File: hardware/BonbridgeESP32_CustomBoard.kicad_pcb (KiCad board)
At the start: 2 copper layers, 55 x 25 mm, 13 parts, among them J1 RJ45_MagJack_10/100M, J2 USB-C_PROG, J3 24V_IN, J4 PRINTER_USB, U1 ESP32-S3-WROOM-1U (IPEX), U2 W5500, U3 Buck_24V_to_5V_3A, U4 LDO_3.3V_600mA

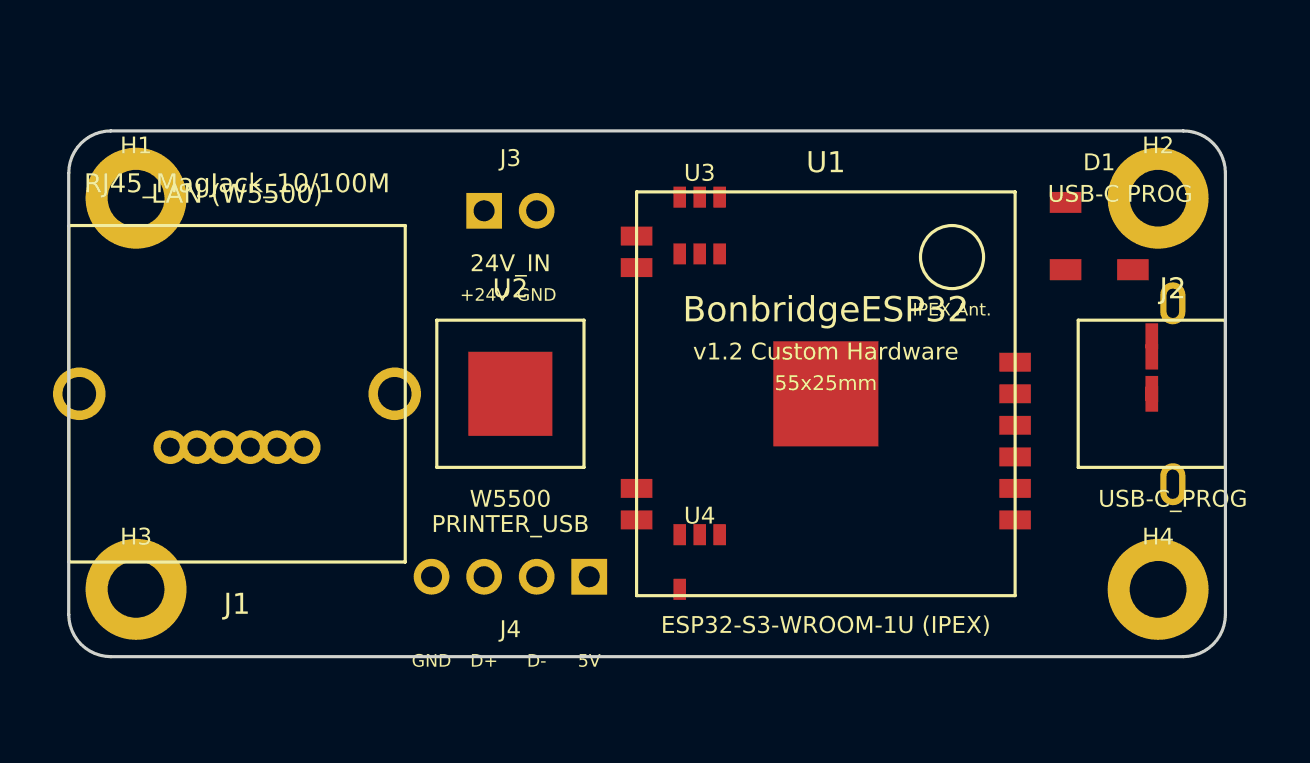
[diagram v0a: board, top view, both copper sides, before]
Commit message: hardware: update KiCad board layout (RJ45 on bottom long edge, USB-C opposite on top, JST top-left side by side)
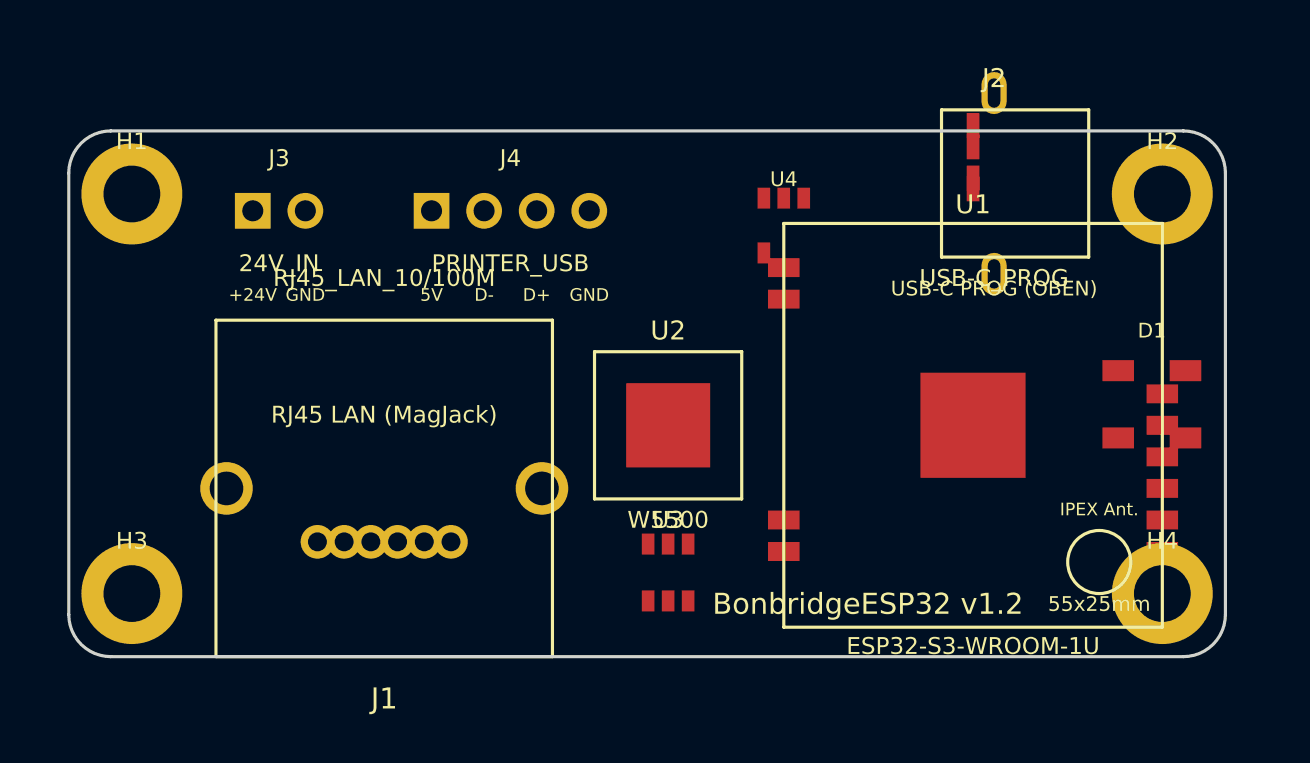
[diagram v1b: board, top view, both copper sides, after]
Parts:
- J1: value RJ45_MagJack_10/100M -> RJ45_LAN_10/100M
- U1: value ESP32-S3-WROOM-1U (IPEX) -> ESP32-S3-WROOM-1U
- moved J4 17.4 mm to (121.0, 103.8), turned to 0 degrees
- moved U3 16.6 mm to (128.5, 121.0)
- moved U4 16.5 mm to (134.0, 104.5)
- moved J2 13.1 mm to (144.0, 102.5), turned to 180 degrees
- moved J3 11.0 mm to (110.0, 103.8)
- moved D1 8.38 mm to (151.5, 113.0)
- moved J1 8.32 mm to (115.0, 117.0), turned to 90 degrees
- moved U2 7.65 mm to (128.5, 114.0)
- moved U1 7.16 mm to (143.0, 114.0)
- moved H1 0.28 mm to (103.0, 103.0)
- moved H3 0.28 mm to (103.0, 122.0)
- moved H2 0.28 mm to (152.0, 103.0)
- moved H4 0.28 mm to (152.0, 122.0)
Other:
- board text added: "BonbridgeESP32 v1.2"
- board text added: "RJ45 LAN (MagJack)"
- board text added: "USB-C PROG (OBEN)"
- board text removed: "BonbridgeESP32"
- board text removed: "LAN (W5500)"
- board text removed: "USB-C PROG"
- board text removed: "v1.2 Custom Hardware"

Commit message: hardware: fix KiCad 10 parsing error, add 3mm RJ45 overhang, and add 3D board renders
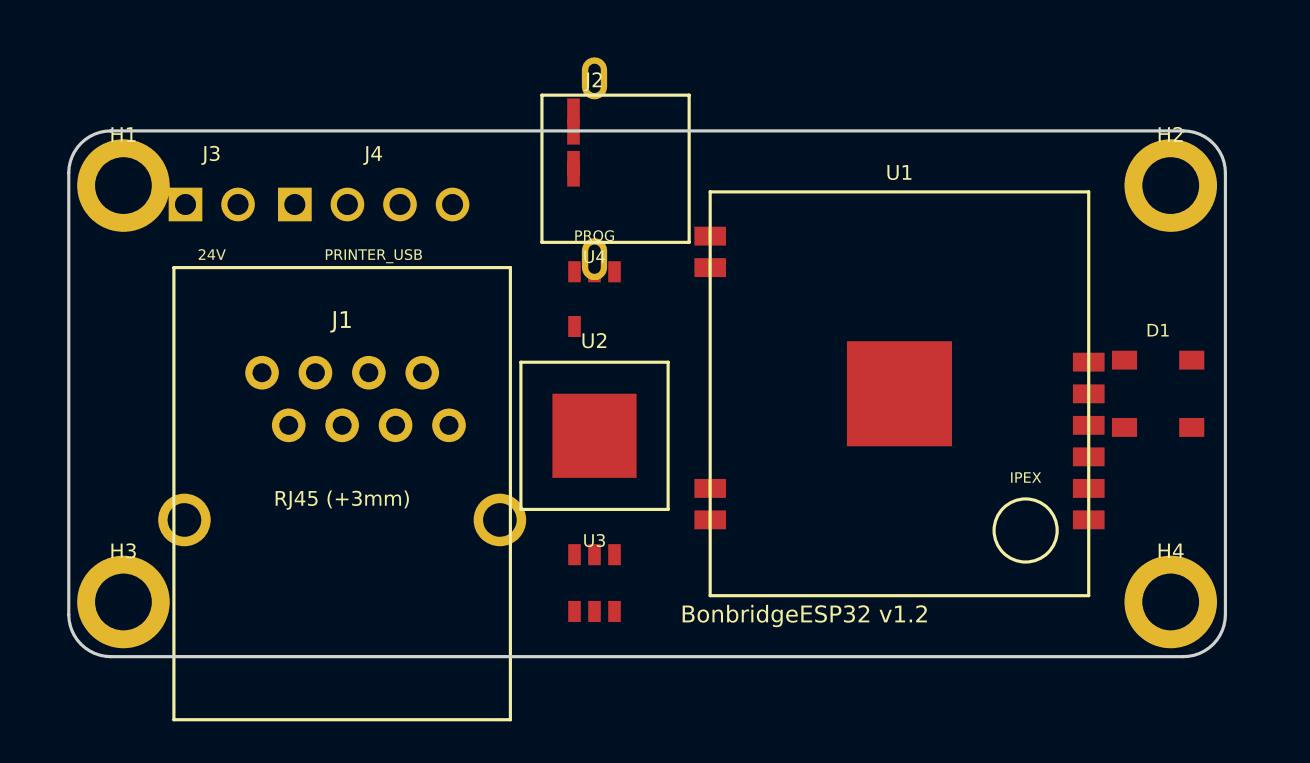
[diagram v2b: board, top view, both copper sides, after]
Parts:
- D1: value WS2812B (RGB) -> RGB
- J1: value RJ45_LAN_10/100M -> RJ45 (+3mm)
- J2: value USB-C_PROG -> PROG
- J3: value 24V_IN -> 24V
- U3: value Buck_24V_to_5V_3A -> Buck
- U4: value LDO_3.3V_600mA -> 3.3V
- moved J2 19.0 mm to (125.0, 101.8)
- moved U4 9.66 mm to (125.0, 108.0)
- moved J4 6.51 mm to (114.5, 103.5)
- moved U1 3.81 mm to (139.5, 112.5)
- moved U2 3.54 mm to (125.0, 114.5)
- moved U3 3.54 mm to (125.0, 121.5)
- moved J3 3.21 mm to (106.8, 103.5)
- moved J1 2.06 mm to (113.0, 117.5), turned to 0 degrees
- moved D1 0.58 mm to (151.8, 112.5)
- moved H1 0.57 mm to (102.6, 102.6)
- moved H2 0.57 mm to (152.4, 102.6)
- moved H3 0.57 mm to (102.6, 122.4)
- moved H4 0.57 mm to (152.4, 122.4)
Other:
- board text removed: "55x25mm"
- board text removed: "RJ45 LAN (MagJack)"
- board text removed: "USB-C PROG (OBEN)"

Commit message: feat(hardware): populate complete component layout with 0 DRC violations and 3D preview
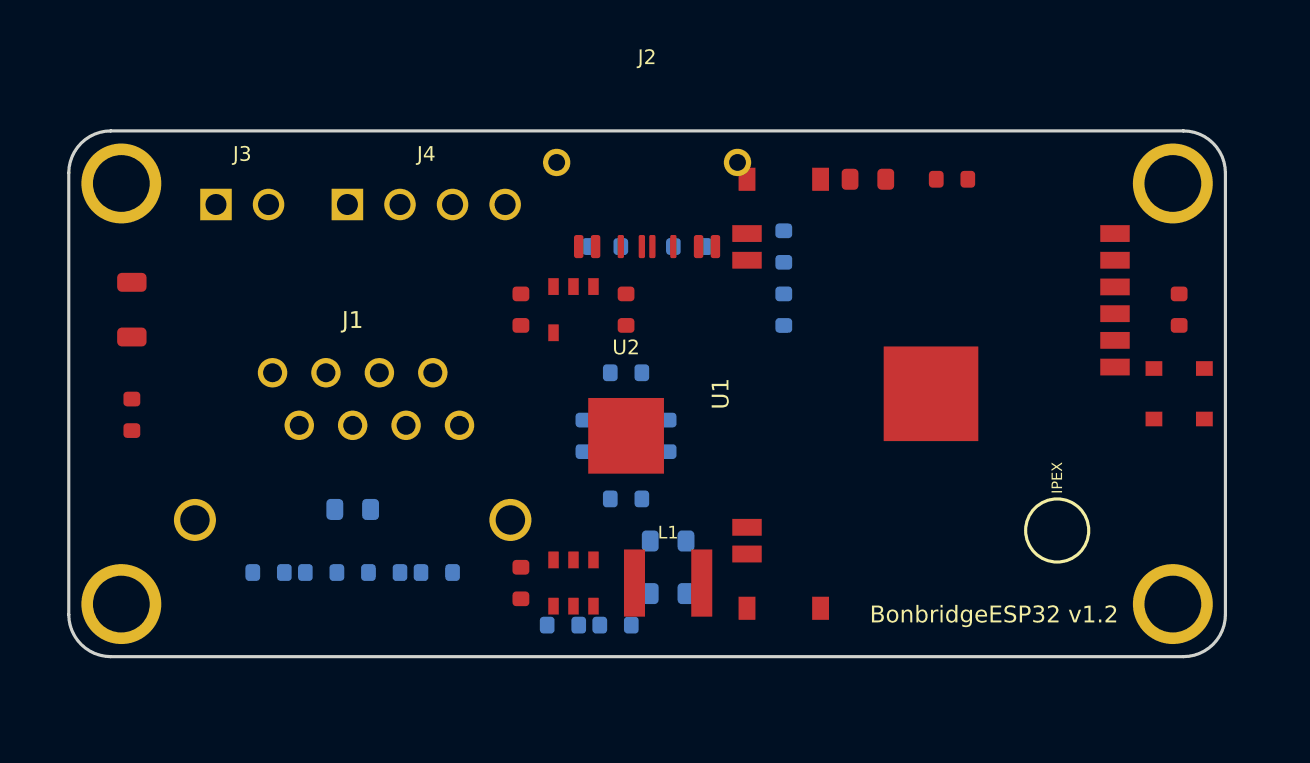
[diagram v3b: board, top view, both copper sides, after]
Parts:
- added C1: 10uF/50V, Capacitor_SMD:C_1206_3216Metric, F.Cu at (103.0, 108.5)
- added C10: 100nF, Resistor_SMD:R_0603_1608Metric, B.Cu at (126.5, 111.5)
- added C11: 100nF, Resistor_SMD:R_0603_1608Metric, B.Cu at (126.5, 117.5)
- added C14: 10nF/2kV, Capacitor_SMD:C_0805_2012Metric, B.Cu at (113.5, 118.0)
- added C15: 10uF, Capacitor_SMD:C_0805_2012Metric, F.Cu at (138.0, 102.3)
- added C16: 100nF, Resistor_SMD:R_0603_1608Metric, F.Cu at (142.0, 102.3)
- added C17: 1uF_EN, Resistor_SMD:R_0603_1608Metric, B.Cu at (134.0, 108.5)
- added C18: 100nF, Resistor_SMD:R_0603_1608Metric, F.Cu at (152.8, 108.5)
- added C2: 100nF, Resistor_SMD:R_0603_1608Metric, F.Cu at (103.0, 113.5)
- added C3: 100nF_BOOT, Resistor_SMD:R_0603_1608Metric, F.Cu at (121.5, 121.5)
- added C4: 22uF_5V, Capacitor_SMD:C_0805_2012Metric, B.Cu at (128.5, 122.0)
- added C5: 22uF_5V, Capacitor_SMD:C_0805_2012Metric, B.Cu at (128.5, 119.5)
- added C6: 4.7uF_IN, Resistor_SMD:R_0603_1608Metric, F.Cu at (121.5, 108.5)
- added C7: 4.7uF_OUT, Resistor_SMD:R_0603_1608Metric, F.Cu at (126.5, 108.5)
- added L1: 4.7uH, Inductor_SMD:L_Bourns-SRN4018, F.Cu at (128.5, 121.5)
- added R1: 100k_FB, Resistor_SMD:R_0603_1608Metric, B.Cu at (123.5, 123.5)
- added R11: 5.1k_CC1, Resistor_SMD:R_0603_1608Metric, B.Cu at (125.5, 105.5)
- added R12: 5.1k_CC2, Resistor_SMD:R_0603_1608Metric, B.Cu at (129.5, 105.5)
- added R13: 10k_EN, Resistor_SMD:R_0603_1608Metric, B.Cu at (134.0, 105.5)
- added R2: 13.3k_FB, Resistor_SMD:R_0603_1608Metric, B.Cu at (126.0, 123.5)
- added R3: 12.4k_BIAS, Resistor_SMD:R_0603_1608Metric, B.Cu at (124.5, 114.5)
- added R4: 10k_RST, Resistor_SMD:R_0603_1608Metric, B.Cu at (128.5, 114.5)
- added R5: 49.9R, Resistor_SMD:R_0603_1608Metric, B.Cu at (109.5, 121.0)
- added R6: 49.9R, Resistor_SMD:R_0603_1608Metric, B.Cu at (112.0, 121.0)
- added R7: 49.9R, Resistor_SMD:R_0603_1608Metric, B.Cu at (115.0, 121.0)
- added R8: 49.9R, Resistor_SMD:R_0603_1608Metric, B.Cu at (117.5, 121.0)
- added SW1: RESET, Button_Switch_SMD:SW_Push_SPST_NO_Alps_SKRK, F.Cu at (134.0, 102.3)
- added SW2: BOOT, Button_Switch_SMD:SW_Push_SPST_NO_Alps_SKRK, F.Cu at (134.0, 122.7)
- J2: value PROG -> USB-C; footprint Connector_USB:USB_C_Receptacle_GCT_USB4085 -> Connector_USB:USB_C_Receptacle_HRO_TYPE-C-31-M-12
- J3: value 24V -> 24V_IN
- moved J2 2.52 mm to (127.5, 101.5)
- moved J4 2.50 mm to (117.0, 103.5)
- moved U1 1.50 mm to (141.0, 112.5), turned to 90 degrees
- moved U2 1.50 mm to (126.5, 114.5)
- moved J3 1.45 mm to (108.2, 103.5)
- moved U4 1.12 mm to (124.0, 108.5)
- moved D1 1.00 mm to (152.8, 112.5)
- moved U3 1.00 mm to (124.0, 121.5)
- moved J1 0.50 mm to (113.5, 117.5)
- moved H1 0.14 mm to (102.5, 102.5)
- moved H2 0.14 mm to (152.5, 102.5)
- moved H3 0.14 mm to (102.5, 122.5)
- moved H4 0.14 mm to (152.5, 122.5)
